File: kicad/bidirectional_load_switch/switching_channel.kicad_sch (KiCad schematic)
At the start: 14 parts, among them U201 SN74LVC1G17DCKR, U202 UCC23313DWYR, U203 SISS94DN-T1-GE3, U204 SISS94DN-T1-GE3

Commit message: i hate layouts
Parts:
- added C205: 100n, Capacitor_SMD:C_0603_1608Metric, symbol Device:C_Small
- added U205: SN74LVC1G08DCKR, and_gate_SN74LVC1G08DCKR:DCK5, symbol and_gate_SN74LVC1G08DCKR:SN74LVC1G08DCKR
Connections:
- net 3V3: now also C205.1, U205.5 (VCC)
- net GND: now also C205.2, U205.3 (GND)
- net PWM: now also U205.1 (A); no longer LED201.2, U201.2 (A)
- net ANODE: no longer names the net of R202.2, U202.1 (ANODE)
- net BOUT: no longer names the net of R202.1, U201.4 (Y)
- net VOUT: no longer names the net of R204.1, R205.1, U202.5 (VOUT)
- new net: LED201.2, U201.2 (A), U205.4 (Y)
- new net ~{fault}: U205.2 (B)
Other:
- company: (none) -> University of Wisconsin-Platteville
- moved on the sheet: C201, C202, C203, C204, LED201, R201, R202, R203, R204, R205, U201, U202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

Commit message: almost
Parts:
- removed U203, U204: SISS94DN-T1-GE3, mosfet_SISS94DN-T1-GE3:MOSFET_3DN-T1-GE3_VIS, symbol mosfet_SISS94DN-T1-GE3:SISS94DN-T1-GE3
- added U204, U205: STD16N60M6, mosfet_STD16N60M6:DPAKTO-252_STM, symbol mosfet_STD16N60M6:STD16N60M6
- renumbered C205 to C201, C201 to C202, C202 to C203, C203 to C204, C204 to C205, U205 to U201, U201 to U202, U202 to U203
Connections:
- net Earth: now also U205.2
- net GNDPWR: now also U204.3, U205.3
- net RIN: now also U204.2
- net VG1: no longer names the net of R204.2
- net VG1: now also U204.1
- net VG2: no longer names the net of R205.2
- net VG2: now also U205.1

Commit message: needs review
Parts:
- added C202: 100n, Capacitor_SMD:C_0603_1608Metric, symbol Device:C_Small
- C201: value 100n -> 1u
- U201: footprint and_gate_SN74LVC1G08DCKR:DCK5 -> DCK5
- U204: footprint mosfet_STD16N60M6:DPAKTO-252_STM -> DPAKTO-252_STM
- renumbered C202 to C203, C203 to C204, C204 to C205, C205 to C206
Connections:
- net 3V3: now also C202.1
- net GND: now also C202.2

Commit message: ready for order
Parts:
- R201: value 150 -> 220
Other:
- moved on the sheet: C201, C202, C205, C206, LED201, R201, R202, R203, R204, R205, U201, U203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

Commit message: updated gerbers
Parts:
- LED201: value B1911PG--20D000514U1930 -> ~; MPN (none) -> B1911PG--20D000514U1930
- U201: value SN74LVC1G08DCKR -> ~; footprint DCK5 -> and_gate_SN74LVC1G08DCKR:DCK5; MPN (none) -> SN74LVC1G08DCKR
- U202: value SN74LVC1G17DCKR -> ~; MPN (none) -> SN74LVC1G17DCKR
- U203: value UCC23313DWYR -> ~; MPN (none) -> UCC23313DWYR
- U204: value STD16N60M6 -> ~; footprint DPAKTO-252_STM -> mosfet_STD16N60M6:DPAKTO-252_STM; MPN (none) -> STD16N60M6
- U205: value STD16N60M6 -> ~; MPN (none) -> STD16N60M6
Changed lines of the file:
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@@
 		(on_board yes)
 		(dnp no)
-		(fields_autoplaced yes)
 		(property "Reference" "U204"
 			(at 234.95 78.2319 0)
@@
 			)
 		)
-		(property "Value" "STD16N60M6"
+		(property "Value" "~"
 			(at 234.95 80.7719 0)
 			(effects
@@
 				)
 				(justify left)
-			)
-		)
-		(property "Footprint" "DPAKTO-252_STM"
+				(hide yes)
+			)
+		)
+		(property "Footprint" "mosfet_STD16N60M6:DPAKTO-252_STM"
 			(at 209.804 61.468 0)
 			(effects
@@
 			)
 		)
-		(property "Datasheet" "STD16N60M6"
+		(property "Datasheet" "https://www.st.com/resource/en/datasheet/std16n60m6.pdf"
 			(at 209.296 58.166 0)
 			(effects
@@
 				)
 				(hide yes)
+			)
+		)
+		(property "MPN" "STD16N60M6"
+			(at 241.3 81.026 0)
+			(effects
+				(font
+					(size 1.27 1.27)
+				)
 			)
 		)
@@
 		(on_board yes)
 		(dnp no)
-		(fields_autoplaced yes)
 		(property "Reference" "U205"
 			(at 234.95 109.7278 0)
@@
 			)
 		)
-		(property "Value" "STD16N60M6"
+		(property "Value" "~"
 			(at 234.95 112.2678 0)
 			(effects
@@
 				)
 				(justify left)
+				(hide yes)
 			)
 		)
@@
 			)
 		)
-		(property "Datasheet" "STD16N60M6"
+		(property "Datasheet" "https://www.st.com/resource/en/datasheet/std16n60m6.pdf"
 			(at 209.296 132.334 0)
 			(effects
@@
 				)
 				(hide yes)
+			)
+		)
+		(property "MPN" "STD16N60M6"
+			(at 241.3 112.014 0)
+			(effects
+				(font
+					(size 1.27 1.27)
+				)
 			)
 		)
@@
 		(on_board yes)
 		(dnp no)
-		(fields_autoplaced yes)
 		(property "Reference" "U203"
 			(at 167.005 69.85 0)
@@
 			)
 		)
-		(property "Value" "UCC23313DWYR"
+		(property "Value" "~"
 			(at 167.005 72.39 0)
 			(effects
@@
 					(size 1.524 1.524)
 				)
+				(hide yes)
 			)
 		)
@@
 				)
 				(hide yes)
+			)
+		)
+		(property "MPN" "UCC23313DWYR"
+			(at 166.878 72.644 0)
+			(effects
+				(font
+					(size 1.27 1.27)
+				)
 			)
 		)
@@
 			)
 		)
-		(property "Value" "B1911PG--20D000514U1930"
+		(property "Value" "~"
 			(at 49.022 88.9 90)
 			(effects
@@
 			)
 		)
-		(property "Datasheet" "B1911PG--20D000514U1930"
+		(property "Datasheet" "https://mm.digikey.com/Volume0/opasdata/d220001/medias/docus/3777/B1911PG--20D000514U1930.pdf"
 			(at 86.36 81.28 0)
 			(effects
@@
 				)
 				(hide yes)
+			)
+		)
+		(property "MPN" "B1911PG--20D000514U1930"
+			(at 94.742 94.996 0)
+			(effects
+				(font
+					(size 1.27 1.27)
+				)
 			)
 		)
@@
 		(dnp no)
 		(property "Reference" "U201"
-			(at 67.056 73.914 0)
-			(effects
-				(font
-					(size 1.524 1.524)
-				)
-			)
-		)
-		(property "Value" "SN74LVC1G08DCKR"
+			(at 59.436 64.516 0)
+			(effects
+				(font
+					(size 1.524 1.524)
+				)
+			)
+		)
+		(property "Value" "~"
 			(at 77.47 76.2314 0)
 			(effects
@@
 			)
 		)
-		(property "Footprint" "DCK5"
+		(property "Footprint" "and_gate_SN74LVC1G08DCKR:DCK5"
 			(at 39.37 62.738 0)
 			(effects
@@
 			)
 		)
-		(property "Datasheet" "SN74LVC1G08DCKR"
+		(property "Datasheet" "https://www.ti.com/general/docs/suppproductinfo.tsp?distId=10&gotoUrl=https%3A%2F%2Fwww.ti.com%2Flit%2Fgpn%2Fsn74lvc1g08"
 			(at 40.132 65.786 0)
 			(effects
@@
 				)
 				(hide yes)
+			)
+		)
+		(property "MPN" "SN74LVC1G08DCKR"
+			(at 59.182 66.802 0)
+			(effects
+				(font
+					(size 1.27 1.27)
+				)
 			)
 		)
@@
 		(on_board yes)
 		(dnp no)
-		(fields_autoplaced yes)
 		(property "Reference" "U202"
 			(at 112.395 69.85 0)
@@
 			)
 		)
-		(property "Value" "SN74LVC1G17DCKR"
+		(property "Value" "~"
 			(at 112.395 72.39 0)
 			(effects
@@
 					(size 1.524 1.524)
 				)
+				(hide yes)
 			)
 		)
@@
 			)
 		)
+		(property "MPN" "SN74LVC1G17DCKR"
+			(at 112.268 72.644 0)
+			(effects
+				(font
+					(size 1.27 1.27)
+				)
+			)
+		)

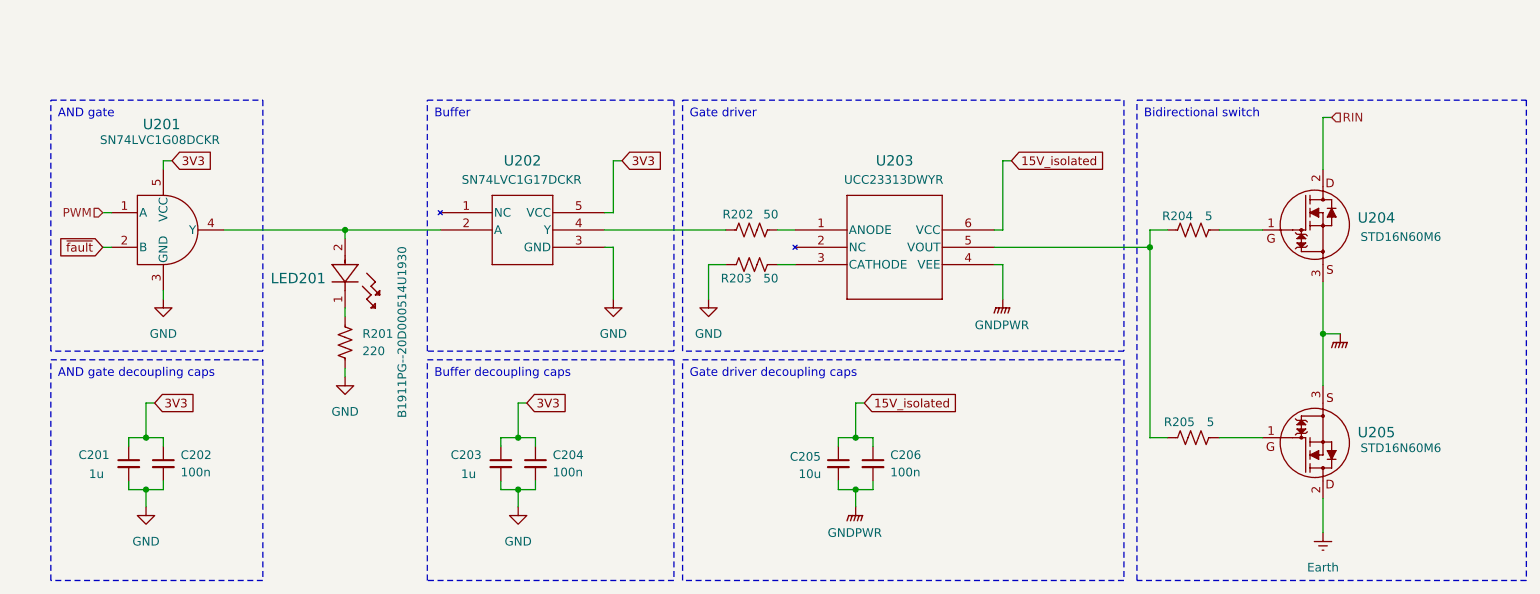
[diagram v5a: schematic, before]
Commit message: removed redundant buffer
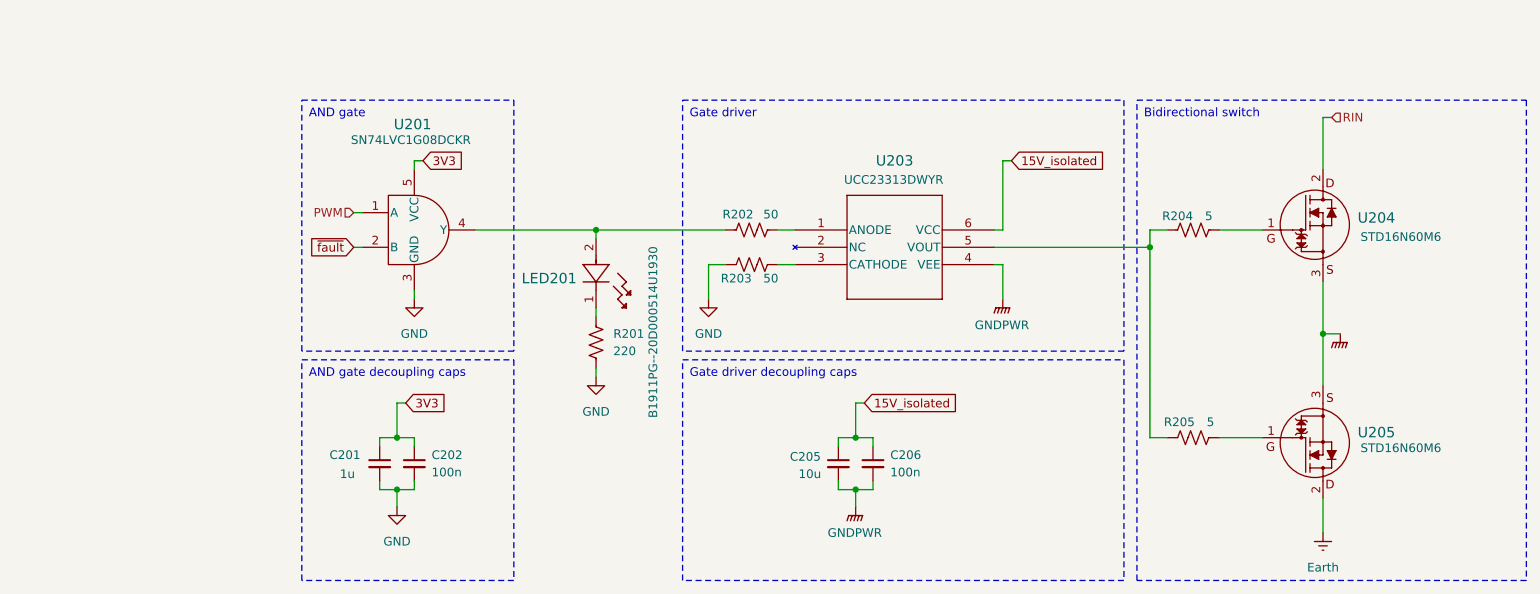
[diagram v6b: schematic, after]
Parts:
- removed C203: 1u, Capacitor_SMD:C_0603_1608Metric, symbol Device:C_Small
- removed C204: 100n, Capacitor_SMD:C_0603_1608Metric, symbol Device:C_Small
- removed U202: ~, buffer_SN74LVC1G17DCKR:DCK5, symbol buffer_SN74LVC1G17DCKR:SN74LVC1G17DCKR
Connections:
- net at LED201.2, U201.4 (Y): now also R202.1
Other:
- moved on the sheet: C201, C202, LED201, R201, U201
